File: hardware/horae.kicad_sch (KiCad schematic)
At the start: 66 parts, among them J1 FH34SRJ-18S-0.5SH(50), Q1 AO3400A, SW1 UP/BOOT, SW2 DOWN, SW3 MENU, SW4 BACK, U1 ESP32-S3FN8, U2 TP4054, U3 RT9080-33, U4 USBLC6-2P6, U5 RV-3032-C7, U6 BMA400, Y1 40MHz 15pF

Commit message: Rev A: hand-routed 50-ohm RF feed, antenna clear of glass, standard vias, cost breakdown; splash-resistant PETG-CF case with TPU gaskets and PETG RF window
Co-Authored-By: Claude Opus 5.5 <noreply@anthropic.com>
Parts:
- C1, C2: value 22pF -> 24pF; LCSC C272881 -> C285108
- D1, D2, D3: value 1N5819WS -> B5819WS; LCSC C2927280 -> C64886
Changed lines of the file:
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@@
           (size 1.27 1.27))
         (justify left)))
-    (property "Value" "22pF"
+    (property "Value" "24pF"
       (at 119.89 49.49 0)
       (effects
@@
         (justify left)
         (hide yes)))
-    (property "LCSC" "C272881"
+    (property "LCSC" "C285108"
       (at 121.92 43.18 0)
       (effects
@@
           (size 1.27 1.27))
         (justify left)))
-    (property "Value" "22pF"
+    (property "Value" "24pF"
       (at 142.75 49.49 0)
       (effects
@@
         (justify left)
         (hide yes)))
-    (property "LCSC" "C272881"
+    (property "LCSC" "C285108"
       (at 144.78 43.18 0)
       (effects
@@
           (size 1.27 1.27))
         (justify left)))
-    (property "Value" "1N5819WS"
+    (property "Value" "B5819WS"
       (at 547.37 44.41 0)
       (effects
@@
         (justify left)
         (hide yes)))
-    (property "LCSC" "C2927280"
+    (property "LCSC" "C64886"
       (at 551.18 40.64 0)
       (effects
@@
           (size 1.27 1.27))
         (justify left)))
-    (property "Value" "1N5819WS"
+    (property "Value" "B5819WS"
       (at 420.37 107.91 0)
       (effects
@@
         (justify left)
         (hide yes)))
-    (property "LCSC" "C2927280"
+    (property "LCSC" "C64886"
       (at 424.18 104.14 0)
       (effects
@@
           (size 1.27 1.27))
         (justify left)))
-    (property "Value" "1N5819WS"
+    (property "Value" "B5819WS"
       (at 448.31 107.91 0)
       (effects
@@
         (justify left)
         (hide yes)))
-    (property "LCSC" "C2927280"
+    (property "LCSC" "C64886"
       (at 452.12 104.14 0)
       (effects

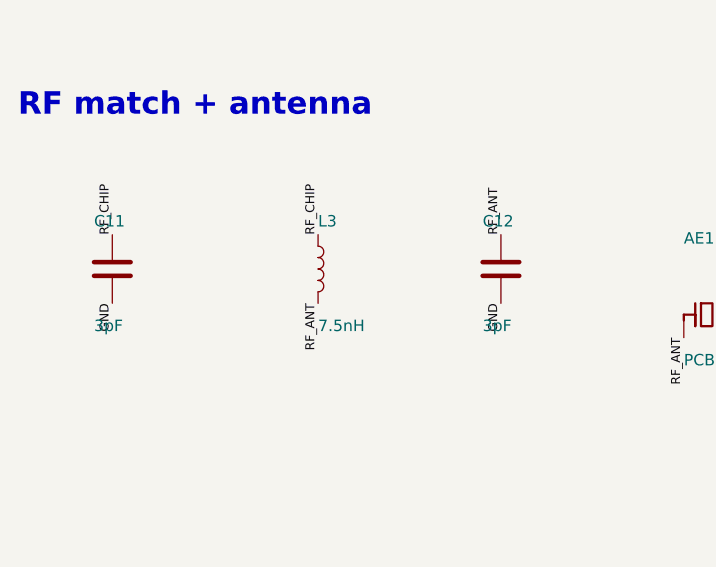
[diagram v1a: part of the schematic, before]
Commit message: Rev A: antenna trimmed 6.64 mm + re-matched from openEMS sim (C11 0.9p, L3 0.6n, C12 DNP); timeline entry with review renders
Co-Authored-By: Claude Opus 5.5 <noreply@anthropic.com>
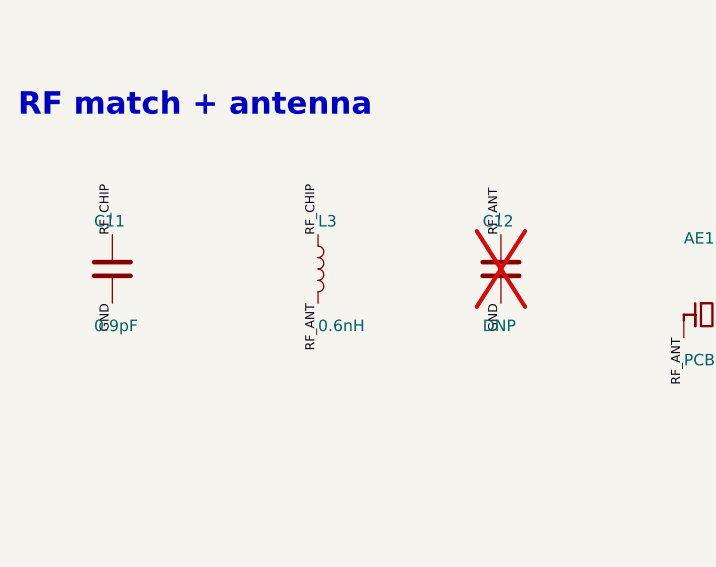
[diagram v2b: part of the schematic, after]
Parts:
- C11: value 3pF -> 0.9pF; LCSC C237430 -> C471401
- C12: value 3pF -> DNP; LCSC C237430 -> (none); now not fitted
- L3: value 7.5nH -> 0.6nH; LCSC C6890513 -> C77699
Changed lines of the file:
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@@
           (size 1.27 1.27))
         (justify left)))
-    (property "Value" "3pF"
+    (property "Value" "0.9pF"
       (at 28.45 273.01 0)
       (effects
@@
         (justify left)
         (hide yes)))
-    (property "LCSC" "C237430"
+    (property "LCSC" "C471401"
       (at 30.48 266.70 0)
       (effects
@@
           (size 1.27 1.27))
         (justify left)))
-    (property "Value" "7.5nH"
+    (property "Value" "0.6nH"
       (at 53.34 273.01 0)
       (effects
@@
         (justify left)
         (hide yes)))
-    (property "LCSC" "C6890513"
+    (property "LCSC" "C77699"
       (at 53.34 266.70 0)
       (effects
@@
     (in_bom yes)
     (on_board yes)
-    (dnp no)
+    (dnp yes)
     (property "Reference" "C12"
       (at 71.63 261.39 0)
@@
           (size 1.27 1.27))
         (justify left)))
-    (property "Value" "3pF"
+    (property "Value" "DNP"
       (at 71.63 273.01 0)
       (effects
@@
       (at 73.66 266.70 0)
       (effects
-        (font
-          (size 1.27 1.27))
-        (justify left)
-        (hide yes)))
-    (property "LCSC" "C237430"
-      (at 73.66 266.70 0)
-      (effects

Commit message: Rev A: haptics back (spring-contact coin ERM + CJ3134K), LIS2DUX12 replaces BMA400 (-$10.9/board), GND escape vias, hole-to-hole spacing; DRC clean
Co-Authored-By: Claude Opus 5.5 <noreply@anthropic.com>
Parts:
- added D4: B5819WS, Diode_SMD:D_SOD-323, symbol Device:D_Schottky
- added Q2: CJ3134K, horae:SOT-723_L1.2-W0.8-P0.40-LS1.2-BR, symbol horae:CJ3134K_C62503
- added R13: 1M, Resistor_SMD:R_0201_0603Metric, symbol Device:R
- added TP7: VBAT, TestPoint:TestPoint_Pad_D1.5mm, symbol Connector:TestPoint
- added TP8: MOT_N, TestPoint:TestPoint_Pad_D1.5mm, symbol Connector:TestPoint
- U6: value BMA400 -> LIS2DUX12; footprint horae:LGA-12_L2.0-W2.0-P0.50-BL -> horae:LGA-12_L2.0-W2.0-P0.50-TL_LIS2DUX12TR; symbol horae:BMA400 -> horae:LIS2DUX12TR; LCSC C437655 -> C17548754
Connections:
- net +3V3: now also U6.2 (CS), U6.9 (VDD); no longer U6.3 (VDDIO), U6.7 (VDD)
- net ACC_INT1: now also U6.12 (INT1); no longer U6.5 (INT1)
- net ACC_INT2: now also U6.11 (INT2); no longer U6.6 (INT2)
- net GND: now also U6.3 (SDO/SA0), U6.6 (GND), U6.7 (RES), Q2.2 (S), R13.2; no longer U6.1 (SDO), U6.9 (GND)
- net I2C_SCL: now also U6.1 (SCL/SPC); no longer U6.12 (SCX)
- net I2C_SDA: now also U6.4 (SDA/SDI/SDO); no longer U6.2 (SDX)
- net VBAT: now also D4.1 (K), TP7.1
- net VIB: now reaches U1.23 (GPIO17)
- net VIB: now also Q2.1 (G), R13.1
- new net MOT_N: D4.2 (A), Q2.3 (D), TP8.1
- no-connect marks 29 -> 27
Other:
- moved on the sheet: C20, TP10, TP11, TP12, TP13, TP9, U6

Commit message: Rev A: capacitive touch (no switches), 6 mm spring-contact motor, full-size battery (25.3x16x2.5), pogo/battery pads in motor-zone corners, PPG hookup pads, RF router class; DRC clean
Co-Authored-By: Claude Opus 5.5 <noreply@anthropic.com>
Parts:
- removed SW1: UP/BOOT, horae:SW-SMD_L3.5-W2.9_EVQ-P7M01P, symbol horae:EVQ-P7M01P
- removed SW2: DOWN, horae:SW-SMD_L3.5-W2.9_EVQ-P7M01P, symbol horae:EVQ-P7M01P
- removed SW3: MENU, horae:SW-SMD_L3.5-W2.9_EVQ-P7M01P, symbol horae:EVQ-P7M01P
- removed SW4: BACK, horae:SW-SMD_L3.5-W2.9_EVQ-P7M01P, symbol horae:EVQ-P7M01P
- added TCH1: TOUCH_UP, horae:TouchPad_4.0x1.6mm, symbol Connector:TestPoint
- added TCH2: TOUCH_DOWN, horae:TouchPad_4.0x1.6mm, symbol Connector:TestPoint
- added TCH3: TOUCH_MENU, horae:TouchPad_4.0x1.6mm, symbol Connector:TestPoint
- added TCH4: TOUCH_BACK, horae:TouchPad_4.0x1.6mm, symbol Connector:TestPoint
- added TP14: I2C_SDA, TestPoint:TestPoint_Pad_D1.0mm, symbol Connector:TestPoint
- added TP15: I2C_SCL, TestPoint:TestPoint_Pad_D1.0mm, symbol Connector:TestPoint
- added TP16: PPG_INT, TestPoint:TestPoint_Pad_D1.0mm, symbol Connector:TestPoint
- TP12: value BTN_UP -> BOOT
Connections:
- net ACC_INT1: now also U1.24 (GPIO18); no longer U1.19 (GPIO14)
- net ACC_INT2: now also U1.27 (GPIO21); no longer U1.24 (GPIO18)
- net I2C_SCL: now also TP15.1
- net I2C_SDA: now also TP14.1
- net TOUCH_UP: now reaches U1.8 (GPIO3)
- net TOUCH_UP: now also TCH1.1
- net BTN_BACK renamed TOUCH_BACK
- net TOUCH_BACK: now also TCH4.1
- net BTN_DOWN renamed TOUCH_DOWN
- net TOUCH_DOWN: now also TCH2.1
- net BTN_MENU renamed TOUCH_MENU
- net TOUCH_MENU: now also TCH3.1
- net BTN_UP renamed BOOT
- new net PPG_INT: TP16.1, U1.19 (GPIO14)
- no-connect marks 27 -> 25
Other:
- moved on the sheet: C1, C2, C3, D4, L1, L2, Q2, R13, TP11, TP12, TP13, U1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

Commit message: Rev A: top-port PDM mic (LMD2718T261, GPIO-powered, 0 uA off) in the -X corner; DRC clean
Co-Authored-By: Claude Opus 5.5 <noreply@anthropic.com>
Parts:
- added C31: 100nF, Capacitor_SMD:C_0201_0603Metric, symbol Device:C
- added MIC1: LMD2718T261, horae:MIC-SMD_6P-L2.8-W1.9-P0.98-TL, symbol horae:LMD2718T261-OA1
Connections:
- net GND: now also C31.2, MIC1.1 (GND), MIC1.2 (L/R), MIC1.3 (GND)
- net MIC_VDD: now reaches U1.43 (GPIO38)
- net MIC_VDD: now also C31.1, MIC1.4 (VDD)
- net MIC_CLK: now reaches U1.44 (MTCK)
- net MIC_CLK: now also MIC1.6 (CLK)
- net MIC_DATA: now reaches U1.45 (MTDO)
- net MIC_DATA: now also MIC1.5 (DATA)
- no-connect marks 25 -> 22
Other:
- moved on the sheet: D4, Q2, R13, TCH1, TCH2, TCH3, TCH4

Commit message: Rev A slim: 33.8 x 16.2 x 0.6 mm board, case under a Charge 3 (35.6 x 18.0 x 7.05)
- Board: 16.2 mm wide (was 18.0), 2.8 mm antenna zone past the glass, 0.6 mm 4-layer;
  ERC 0, DRC 0 errors / 0 warnings / 0 unconnected, every signal routed on the first pass.
- Tallest part 1.0 mm (was 1.2): PMZ390UN MOSFETs (SOT-883), PMEG3005EL Schottkys
  (SOD-882), FNR3010 47 uH 3x3x1.0, 0402 4.7 uF/25 V; SSD1681 reference values.
- RTC IC dropped: 32.768 kHz crystal on GPIO15/16 runs the ESP32 RTC (Watchy v3 /
  Yatchy approach, -$3.44).
- Power: BQ25101 charger (75 nA drain, 28 V input, 24 mA for the 40-55 mAh cell) and
  TPS62840 buck (60 nA Iq, 267k VSET -> 3.3 V) replace TP4054 + RT9080; hand-placed buck cell.
- GPIO plan: display + I2C on the U1 side facing J1 (RTC GPIOs, ULP-drivable), touch /
  interrupts / haptics / ADC on the antenna side; USB straight to the ESP32.
- RF match from the openEMS re-run: C11 0.3 pF, L3 1.2 nH (C12 DNP).
- Fixes: C28 footprint/part mismatch (0201 pads, 0402 part); route.py took the first rule
  area as the antenna keep-out (pours on F/In2/B stopped at x = -7.5); RF shunt vias get
  their own stub; build.sh died on a perfect route (grep -c exit 1); broken EasyEDA pads
  on the 0603 inductor; silk moved to fab, battery +/- marks on the bottom.
- README: Standard PCBA is required (0201s, 0.4 mm WCSPs), corrected cost, real battery
  capacity (40-55 mAh), motor/battery soldered, review checklist, GPIO table. cost.py added.

Co-Authored-By: Claude Opus 5.5 <noreply@anthropic.com>
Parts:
- removed C16: 1uF, Capacitor_SMD:C_0201_0603Metric, symbol Device:C
- removed C19: 100nF, Capacitor_SMD:C_0201_0603Metric, symbol Device:C
- removed R7, R8: 22, Resistor_SMD:R_0201_0603Metric, symbol Device:R
- removed TP14: I2C_SDA, TestPoint:TestPoint_Pad_D1.0mm, symbol Connector:TestPoint
- removed TP15: I2C_SCL, TestPoint:TestPoint_Pad_D1.0mm, symbol Connector:TestPoint
- removed TP16: PPG_INT, TestPoint:TestPoint_Pad_D1.0mm, symbol Connector:TestPoint
- removed U5: RV-3032-C7, horae:OSC-SMD_8P-L3.2-W1.5-P0.90-BL, symbol horae:RV-3032-C732.768KHZ-2.5PPM-TA-QC
- added C32, C33: 20pF, Capacitor_SMD:C_0201_0603Metric, symbol Device:C
- added L5: 2.2uH, horae:IND-SMD_L1.6-W0.8, symbol Device:L
- added R5: 10k, Resistor_SMD:R_0201_0603Metric, symbol Device:R
- added R6: 267k, Resistor_SMD:R_0201_0603Metric, symbol Device:R
- added Y2: 32.768kHz 12.5pF, horae:CRYSTAL-SMD_L2.1-W1.2-P1.50, symbol Device:Crystal
- C11: value 0.9pF -> 0.3pF; LCSC C471401 -> C76927
- C15: value 22uF -> 10uF; footprint Capacitor_SMD:C_0603_1608Metric -> Capacitor_SMD:C_0402_1005Metric; LCSC C59461 -> C15525
- C22: footprint Capacitor_SMD:C_0603_1608Metric -> Capacitor_SMD:C_0402_1005Metric; LCSC C69335 -> C2858031
- C28: footprint Capacitor_SMD:C_0201_0603Metric -> Capacitor_SMD:C_0402_1005Metric
- D1, D2, D3, D4: value B5819WS -> PMEG3005EL; footprint Diode_SMD:D_SOD-323 -> horae:SOD-882_L1.0-W0.6-RD; LCSC C64886 -> C282565
- L3: value 0.6nH -> 1.2nH; LCSC C77699 -> C77113
- L4: footprint Inductor_SMD:L_Sunlord_SWPA3012S -> horae:IND-SMD_L3.0-W3.0_FNR3010S; LCSC C83420 -> C167729
- Q1: value AO3400A -> PMZ390UN; footprint Package_TO_SOT_SMD:SOT-23 -> horae:SOT-883-3_L1.0-W0.6-BR; symbol Transistor_FET:AO3400A -> horae:PMZ390UN,315; LCSC C20917 -> C458236
- Q2: value CJ3134K -> PMZ390UN; footprint horae:SOT-723_L1.2-W0.8-P0.40-LS1.2-BR -> horae:SOT-883-3_L1.0-W0.6-BR; symbol horae:CJ3134K_C62503 -> horae:PMZ390UN,315; LCSC C62503 -> C458236
- R2: value 20k -> 5.6k; LCSC C295787 -> C384405
- U2: value TP4054 -> BQ25101; footprint horae:SOT-23-5_L3.0-W1.7-P0.95-LS2.8-BL -> horae:DSBGA-6_L0.9-W1.6-R2-C3-P0.40-BL; symbol horae:TP4054 -> horae:BQ25101YFPR; LCSC C32574 -> C478468
- U3: value RT9080-33 -> TPS62840; footprint horae:TSOT-23-5_L2.9-W1.6-P0.95-LS2.8-BL -> horae:DSBGA-6_L1.4-W1.0-R2-C3-P0.40-BL; symbol horae:RT9080-33GJ5 -> horae:TPS62840YBGR; LCSC C841192 -> C2071139
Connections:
- net ESP_DM is gone; now on net USB_DM: U1.25 (GPIO19/USB_D-)
- net ESP_DP is gone; now on net USB_DP: U1.26 (GPIO20/USB_D+)
- net PPG_INT is gone; now on net EPD_DC: U1.19 (GPIO14)
- net RTC_INT is gone; now on net VIB: U1.10 (GPIO5)
- net +3V3: now also U3.A2 (VOS), L5.2; no longer U3.5 (VOUT)
- net ACC_INT1: now also U1.14 (GPIO9); no longer U1.24 (GPIO18)
- net ACC_INT2: now also U1.13 (GPIO8); no longer U1.27 (GPIO21)
- net BAT_ADC: now also U1.12 (GPIO7); no longer U1.14 (GPIO9)
- net CHG_STAT: now also U1.11 (GPIO6), U2.C1 (~{CHG}); no longer U1.15 (GPIO10), U2.1 (CHRG)
- net EPD_BUSY: now also U1.17 (GPIO12); no longer U1.6 (GPIO1)
- net EPD_CS: now also U1.23 (GPIO17); no longer U1.22 (XTAL_32K_N)
- net EPD_DC: no longer U1.21 (XTAL_32K_P)
- net EPD_MOSI: now also U1.27 (GPIO21); no longer U1.18 (GPIO13)
- net EPD_RES: now also U1.18 (GPIO13); no longer U1.7 (GPIO2)
- net EPD_SCK: now also U1.24 (GPIO18); no longer U1.9 (GPIO4)
- net GND: now also U2.C2 (VSS), U3.A1 (GND), C32.2, C33.2, R5.2, R6.2; no longer U2.2 (GND), U3.2 (GND)
- net I2C_SDA: now also U1.15 (GPIO10); no longer U1.17 (GPIO12)
- net TOUCH_BACK: now also U1.7 (GPIO2); no longer U1.11 (GPIO6)
- net TOUCH_DOWN: now also U1.6 (GPIO1); no longer U1.13 (GPIO8)
- net TOUCH_MENU: now also U1.8 (GPIO3); no longer U1.12 (GPIO7)
- net TOUCH_UP: now also U1.9 (GPIO4); no longer U1.8 (GPIO3)
- net VBAT: now also U2.A1 (OUT), U3.B1 (VIN), U3.C1 (EN); no longer U2.3 (BAT), U3.1 (VIN), U3.3 (EN)
- net VBUS: now also U2.A2 (IN); no longer U2.4 (VCC)
- net VIB: no longer U1.23 (GPIO17)
- net PROG renamed CHG_ISET
- net CHG_ISET: now also U2.B2 (ISET); no longer U2.5 (PROG)
- new net BUCK_SW: L5.1, U3.B2 (SW)
- new net BUCK_VSET: R6.1, U3.C2 (VSET)
- new net CHG_TS: R5.1, U2.B1 (TS)
- new net XTAL32_N: C33.1, U1.22 (XTAL_32K_N), Y2.2
- new net XTAL32_P: C32.1, U1.21 (XTAL_32K_P), Y2.1
- no-connect marks 22 -> 20
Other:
- moved on the sheet: C10, C13, C15, C17, C18, C20, C3, C5, C6, C7, C8, C9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

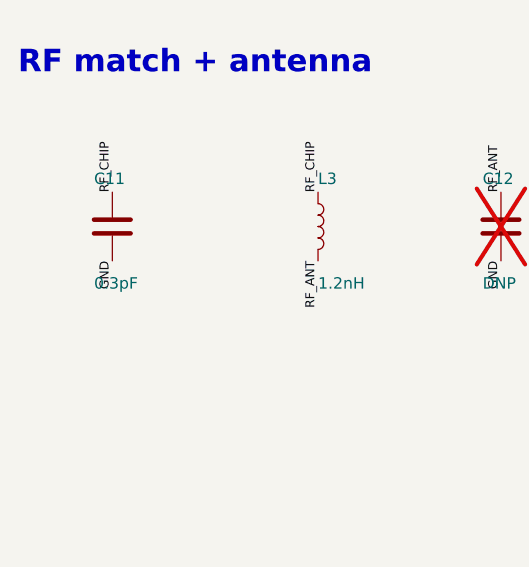
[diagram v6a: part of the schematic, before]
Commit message: Rev A: C11 0.5 pF (RF v3); README for the 6.80 mm two-shell case and magnetic cable
ERC 0, DRC 0 errors / 0 warnings / 0 unconnected.

Co-Authored-By: Claude Opus 5.5 <noreply@anthropic.com>
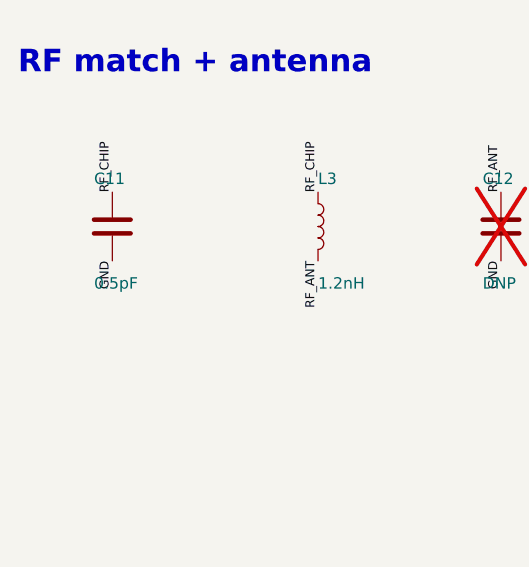
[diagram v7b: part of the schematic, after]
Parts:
- C11: value 0.3pF -> 0.5pF; LCSC C76927 -> C85920
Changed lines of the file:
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@@
           (size 1.27 1.27))
         (justify left)))
-    (property "Value" "0.3pF"
+    (property "Value" "0.5pF"
       (at 28.45 273.01 0)
       (effects
@@
         (justify left)
         (hide yes)))
-    (property "LCSC" "C76927"
+    (property "LCSC" "C85920"
       (at 30.48 266.70 0)
       (effects

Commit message: Pre-order review: board, case and RF reworked; order and assembly guides
Four parallel reviews (schematic/parts, layout/fab, size, sourcing) found
7 blockers, all fixed:
- J1 faced the wrong way (FH34SRJ slot is on the fitting-nail side):
  turned, pins remapped (pad = 19 - display pin), moved +1.7 mm so the
  11.18 mm tail keeps GD's R > 0.5 bend
- CPL now in the gerber frame with JLC rotation offsets (U4, L4)
- TI's 0.23 mm NSMD lands for the BQ25101/TPS62840 WCSPs
- no foreign traces under the touch electrodes (all layers), 510R series
- RF match pads 0.15 mm apart, no paste on C12/AE1
- ESP32 EP per Espressif: vias in the mask webs, none in the paste
- 1-up 70 x 70 mm panel frame (panel.py) for JLC Standard PCBA

Also:
- 0.45/0.2 vias, power classes, decoupling at the pins, crystals on F.Cu,
  USB ESD flow-through, mic DATA/VDD swapped off the ROM-driven pin
- parts: LSCND1608 buck L (1.3 A), PMEG3002AEL, 2.2 uF rail caps, ST
  USBLC6, ISET RC, charger and booster input caps, KYX 40 MHz + 18 pF caps
- I2C on GPIO8/9 and INT on GPIO10/11; LIS2DUX12 now at 0x19
- PCB 33.6 x 16.0 (0.2 mm off every wall in the same case); six crush ribs
- RF v4 on the new layout: L3 1.2 -> 0.8 nH (worst in-band loss 0.78 dB)
- case: FPC loop model per GD, raised hood, ePTFE vent seat, TPU 90A only,
  cell max size, watertight exports, dock wiring diagram
- cost.py on JLC's current Standard fees ($1.53 per line, fixtures, X-ray)
- ORDER.md, ASSEMBLY.md, hardware README rewritten; timeline entry

ERC 0, DRC 0/0/0, JLC capability probe clean, reproducible build.

Co-Authored-By: Claude Opus 5.5 <noreply@anthropic.com>
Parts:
- added C14: 1uF, Capacitor_SMD:C_0201_0603Metric, symbol Device:C
- added C19, C36: 10nF, Capacitor_SMD:C_0201_0603Metric, symbol Device:C
- added C34: 100nF, Capacitor_SMD:C_0201_0603Metric, symbol Device:C
- added C35: 10uF, Capacitor_SMD:C_0402_1005Metric, symbol Device:C
- added R14, R15, R16, R17: 510, Resistor_SMD:R_0201_0603Metric, symbol Device:R
- added R7: 2.7k, Resistor_SMD:R_0201_0603Metric, symbol Device:R
- C1, C2: value 24pF -> 18pF; LCSC C285108 -> C62164
- C13: value 1uF -> 4.7uF/25V; footprint Capacitor_SMD:C_0201_0603Metric -> Capacitor_SMD:C_0402_1005Metric; LCSC C76935 -> C2858031
- C24, C25, C28, C29: value 1uF/25V -> 2.2uF/25V; LCSC C52923 -> C307418
- C32, C33: value 20pF -> 18pF; LCSC C71879 -> C62164
- C6: value 100nF -> 1uF; LCSC C66938 -> C76935
- D1, D2, D3, D4: value PMEG3005EL -> PMEG3002AEL; LCSC C282565 -> C478015
- L3: value 1.2nH -> 0.8nH; LCSC C77113 -> C156227
- L4: footprint horae:IND-SMD_L3.0-W3.0_FNR3010S -> horae:IND-SMD_L3.0-W3.0_SWPA3010S; LCSC C167729 -> C96826
- L5: LCSC C222814 -> C31123918
- R2: value 5.6k -> 6.8k; LCSC C384405 -> C274877
- R3, R4: LCSC C320452 -> C3036920
- TCH1: value TOUCH_UP -> TOUCH_UP_E
- TCH2: value TOUCH_DOWN -> TOUCH_DOWN_E
- TCH3: value TOUCH_MENU -> TOUCH_MENU_E
- TCH4: value TOUCH_BACK -> TOUCH_BACK_E
- TP2: value USB_DM -> USB_DM_POGO
- TP3: value USB_DP -> USB_DP_POGO
- TP6: footprint TestPoint:TestPoint_Pad_2.0x2.0mm -> TestPoint:TestPoint_Pad_D2.0mm
- U1: footprint Package_DFN_QFN:QFN-56-1EP_7x7mm_P0.4mm_EP4x4mm_ThermalVias -> horae:QFN-56-1EP_7x7mm_P0.4mm_EP4x4mm_Espressif
- U4: LCSC C2827693 -> C15999
- Y1: value 40MHz 15pF -> 40MHz 12pF; LCSC C284176 -> C19076867
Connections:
- net +3V3: now also J1.9, U6.3 (SDO/SA0), C34.1, C35.1, C36.1; no longer J1.10
- net ACC_INT1: now also U1.15 (GPIO10); no longer U1.14 (GPIO9)
- net ACC_INT2: now also U1.16 (GPIO11); no longer U1.13 (GPIO8)
- net CHG_ISET: now also R7.1
- net EPD_BUSY: now also J1.15; no longer J1.4
- net EPD_CS: now also J1.12; no longer J1.7
- net EPD_DC: now also J1.13; no longer J1.6
- net EPD_GDR: now also J1.18; no longer J1.1
- net EPD_MOSI: now also J1.10; no longer J1.9
- net EPD_RES: now also J1.14; no longer J1.5
- net EPD_RESE: now also J1.17; no longer J1.2
- net EPD_SCK: now also J1.11; no longer J1.8
- net EPD_VCOM: now also J1.1; no longer J1.18
- net EPD_VDD: now also J1.7; no longer J1.12
- net EPD_VSH1: now also J1.5; no longer J1.14
- net EPD_VSHR: now also J1.16; no longer J1.3
- net EPD_VSL: now also J1.3; no longer J1.16
- net GND: now also J1.8, C14.2, C19.2, C34.2, C35.2, C36.2; no longer J1.11, U6.3 (SDO/SA0)
- net I2C_SCL: now also U1.14 (GPIO9); no longer U1.16 (GPIO11)
- net I2C_SDA: now also U1.13 (GPIO8); no longer U1.15 (GPIO10)
- net MIC_DATA: now also U1.43 (GPIO38); no longer U1.45 (MTDO)
- net MIC_VDD: now also U1.45 (MTDO); no longer U1.43 (GPIO38)
- net PREVGH: now also J1.4; no longer J1.15
- net PREVGL: now also J1.2; no longer J1.17
- net TOUCH_BACK: now also R17.1; no longer TCH4.1
- net TOUCH_DOWN: now also R15.1; no longer TCH2.1
- net TOUCH_MENU: now also R16.1; no longer TCH3.1
- net TOUCH_UP: now also R14.1; no longer TCH1.1
- net USB_DM: no longer TP2.1, U4.3 (I/O2)
- net USB_DP: no longer TP3.1, U4.1 (I/O1)
- net VBAT: now also C14.1
- new net CHG_ISET_RC: C19.1, R7.2
- new net TOUCH_BACK_E: R17.2, TCH4.1
- new net TOUCH_DOWN_E: R15.2, TCH2.1
- new net TOUCH_MENU_E: R16.2, TCH3.1
- new net TOUCH_UP_E: R14.2, TCH1.1
- new net USB_DM_POGO: TP2.1, U4.3 (I/O2)
- new net USB_DP_POGO: TP3.1, U4.1 (I/O1)
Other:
- moved on the sheet: C10, C13, C15, C17, C18, C22, C24, C25, C26, C27, C28, C29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
